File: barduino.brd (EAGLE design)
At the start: 50.3 x 47.4 mm, 28 parts, among them Q2 16MHz

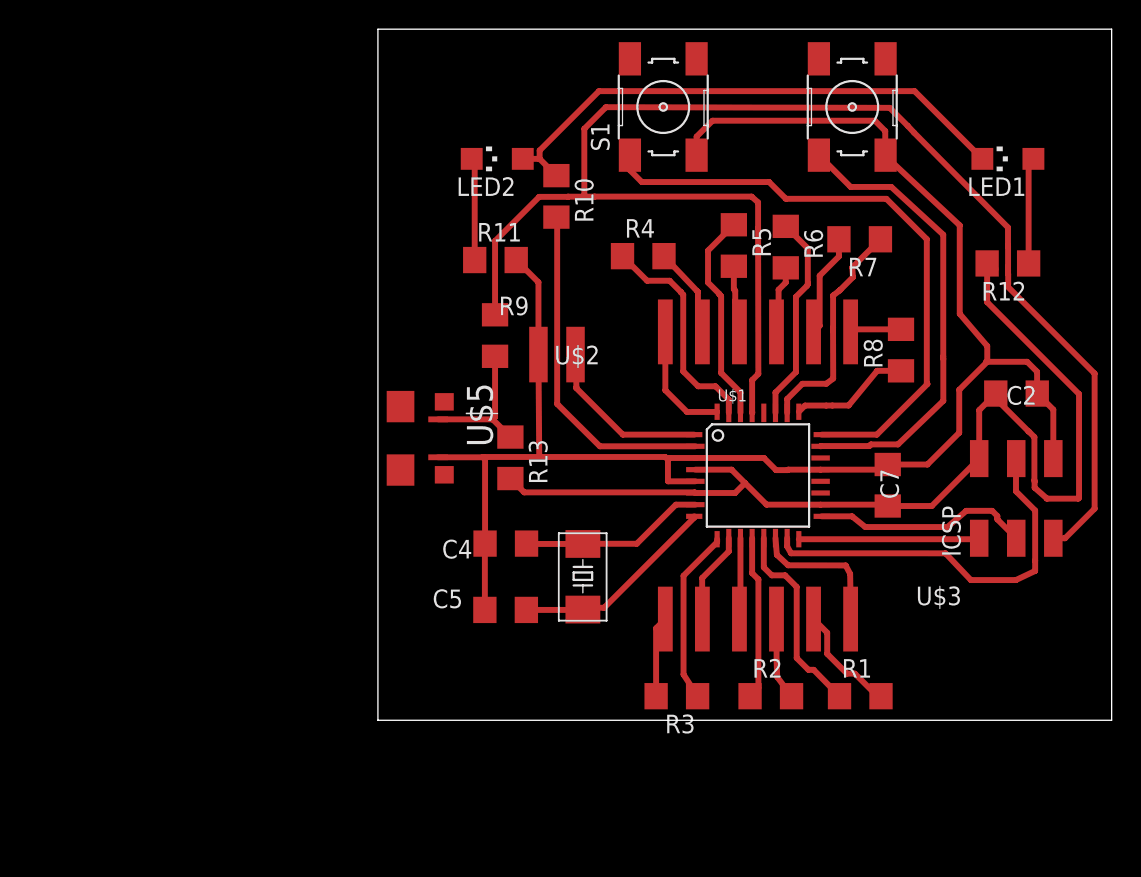
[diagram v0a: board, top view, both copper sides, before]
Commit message: replace crystal with new footprint part
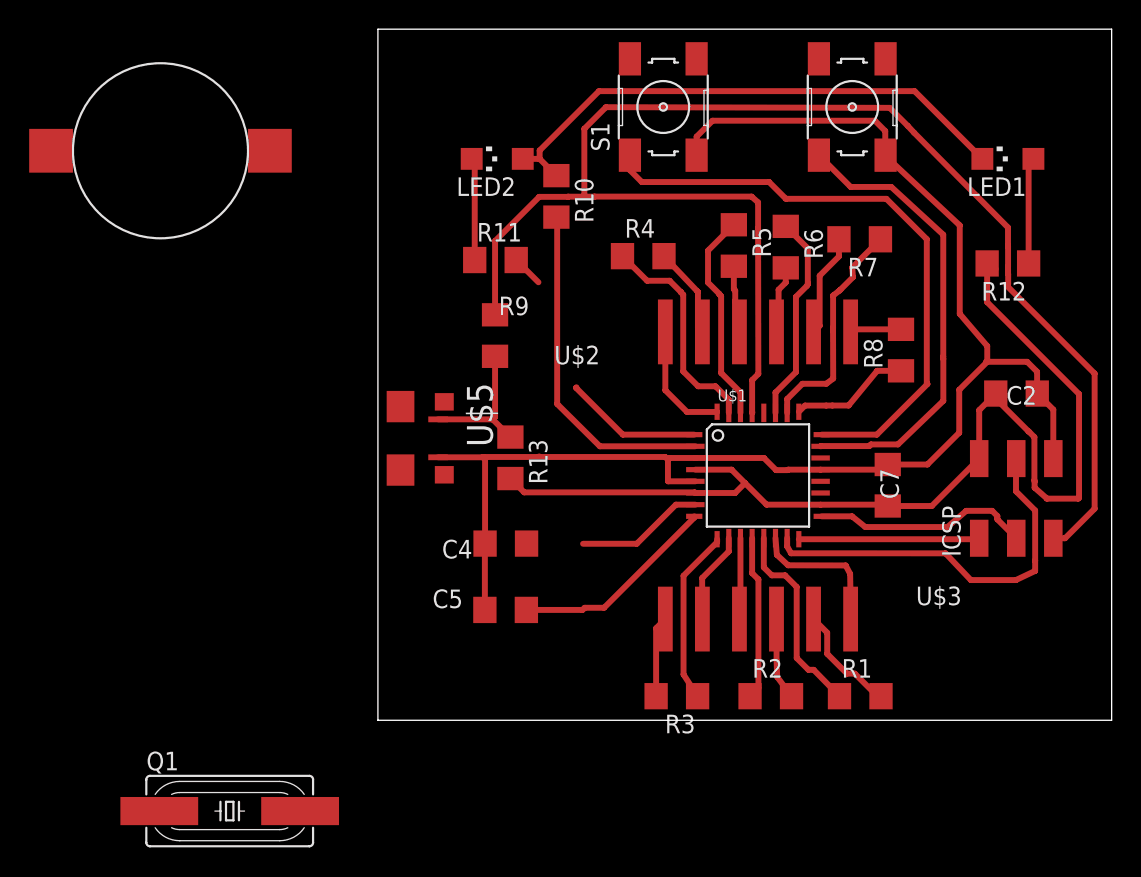
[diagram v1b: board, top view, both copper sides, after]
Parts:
- removed Q2: 16MHz, ng:CS10
- added Q1: 16MHz, crystal:HC49UP
- U$4: device 4-Digit-Clock:BUZZER -> 4-Digit-Clock:CD-1206-SMT
- moved U$4 30.6 mm to (-30.1, 51.4)
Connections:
- net PB6: now also Q1.2; no longer Q2.P$2
- net PB7: now also Q1.1; no longer Q2.P$1
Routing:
- net GND: track 115.3 -> 103.4 mm
- net PB6: track 12.7 -> 8.84 mm
- net D3: track 11.7 -> 9.47 mm
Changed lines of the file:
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@@
 </autorouter>
 <elements>
-<element name="Q2" library="ng" package="CS10" value="16MHz" x="-1.1912" y="22.19458125" smashed="yes" rot="R90">
-<attribute name="VALUE" x="2.2378" y="19.01958125" size="1.27" layer="27" ratio="10" rot="R90"/>
-</element>
 <element name="C4" library="ng" package="1206" value="18pF" x="-6.4744" y="24.42978125" smashed="yes">
 <attribute name="NAME" x="-8.7604" y="24.68378125" size="1.27" layer="25" rot="R180"/>
@@
 <element name="U$2" library="4-Digit-Clock" package="HEADER" value="HEADER" x="10.8103" y="36.7183"/>
 <element name="U$3" library="4-Digit-Clock" package="HEADER" value="HEADER" x="10.8103" y="21.4783" rot="R180"/>
-<element name="U$4" library="4-Digit-Clock" package="BUZZER" value="BUZZER" x="-2.96671875" y="37.3862625" rot="R180"/>
+<element name="U$4" library="4-Digit-Clock" package="CD-1206-SMT" value="BUZZER" x="-30.14471875" y="51.3562625" rot="R180"/>
 <element name="R1" library="resistor" library_urn="urn:adsk.eagle:library:348" package="R1206" package3d_urn="urn:adsk.eagle:package:26062/1" value="" x="17.820640625" y="13.97"/>
 <element name="R2" library="resistor" library_urn="urn:adsk.eagle:library:348" package="R1206" package3d_urn="urn:adsk.eagle:package:26062/1" value="" x="11.689078125" y="13.97"/>
@@
 <element name="U$5" library="4-Digit-Clock" package="DX4R005HJ5-PWR" value="MICRO-USB-PWR" x="-15.24" y="31.645859375" rot="R270"/>
 <element name="R13" library="resistor" library_urn="urn:adsk.eagle:library:348" package="R1206" package3d_urn="urn:adsk.eagle:package:26062/1" value="" x="-6.1595" y="30.30981875" rot="R270"/>
+<element name="Q1" library="crystal" library_urn="urn:adsk.eagle:library:204" package="HC49UP" package3d_urn="urn:adsk.eagle:package:12078/1" value="16MHz" x="-25.4" y="6.096">
+<attribute name="MF" value="" x="-25.4" y="6.096" size="1.778" layer="27" display="off"/>
+<attribute name="MPN" value="" x="-25.4" y="6.096" size="1.778" layer="27" display="off"/>
+<attribute name="OC_FARNELL" value="unknown" x="-25.4" y="6.096" size="1.778" layer="27" display="off"/>
+<attribute name="OC_NEWARK" value="unknown" x="-25.4" y="6.096" size="1.778" layer="27" display="off"/>
+</element>
 </elements>
 <signals>
@@
 <wire x1="4.761140625" y1="30.2983" x2="4.64058125" y2="30.177740625" width="0.4064" layer="1"/>
 <wire x1="19.65190625" y1="50.906009375" x2="19.558" y2="51.054" width="0.4064" layer="1"/>
-<wire x1="-4.183378125" y1="30.406540625" x2="-4.23671875" y2="37.3862625" width="0.4064" layer="1"/>
+<wire x1="-4.183378125" y1="30.406540625" x2="-37.64471875" y2="51.3562625" width="0" layer="19" extent="1-16"/>
 <wire x1="-4.183378125" y1="30.406540625" x2="-4.254496875" y2="30.3659" width="0.4064" layer="1"/>
 <wire x1="-4.254496875" y1="30.3659" x2="4.452421875" y2="30.3659" width="0.4064" layer="1"/>
@@
 <wire x1="-8.0924375" y1="30.3430375" x2="-8.016240625" y2="30.3659" width="0.4064" layer="1"/>
 <contactref element="R11" pad="2"/>
-<wire x1="-4.23671875" y1="37.3862625" x2="-4.23671875" y2="42.341403125" width="0.4064" layer="1"/>
+<wire x1="-37.64471875" y1="51.3562625" x2="-4.23671875" y2="42.341403125" width="0" layer="19" extent="1-16"/>
 <wire x1="-4.23671875" y1="42.341403125" x2="-5.76111875" y2="43.865803125" width="0.4064" layer="1"/>
 <contactref element="U$5" pad="GND"/>
@@
 </signal>
 <signal name="PB7">
-<contactref element="Q2" pad="P$1"/>
 <contactref element="C5" pad="2"/>
 <contactref element="U$1" pad="8"/>
@@
 <wire x1="6.4415" y1="26.210321875" x2="0.26161875" y2="20.030440625" width="0.4064" layer="1"/>
 <wire x1="-1.069340625" y1="20.030440625" x2="0.26161875" y2="20.030440625" width="0.4064" layer="1"/>
-<wire x1="-1.069340625" y1="20.030440625" x2="-1.1912" y2="19.90858125" width="0.4064" layer="1"/>
 <wire x1="-5.0651" y1="19.883175" x2="-1.21660625" y2="19.883175" width="0.4064" layer="1"/>
 <wire x1="-1.21660625" y1="19.883175" x2="-1.069340625" y2="20.030440625" width="0.4064" layer="1"/>
+<contactref element="Q1" pad="1"/>
+<wire x1="-5.0651" y1="19.883175" x2="-30.226" y2="6.096" width="0" layer="19" extent="1-1"/>
 </signal>
 <signal name="RESET">
@@
 </signal>
 <signal name="PB6">
-<contactref element="Q2" pad="P$2"/>
 <contactref element="C4" pad="2"/>
 <wire x1="5.18318125" y1="27.0983" x2="2.5019" y2="24.41701875" width="0.4064" layer="1"/>
 <wire x1="2.5019" y1="24.41701875" x2="-1.1785625" y2="24.41701875" width="0.4064" layer="1"/>
-<wire x1="-1.1785625" y1="24.41701875" x2="-1.1912" y2="24.40438125" width="0.4064" layer="1"/>
-<wire x1="-1.1912" y1="24.40438125" x2="-5.027" y2="24.40438125" width="0.4064" layer="1"/>
 <wire x1="-5.027" y1="24.40438125" x2="-5.0524" y2="24.42978125" width="0.4064" layer="1"/>
 <contactref element="U$1" pad="7"/>
 <wire x1="6.5177" y1="27.0983" x2="5.18318125" y2="27.0983" width="0.4064" layer="1"/>
+<contactref element="Q1" pad="2"/>
+<wire x1="-5.027" y1="24.40438125" x2="-1.1785625" y2="24.41701875" width="0" layer="19" extent="1-1"/>
+<wire x1="-20.574" y1="6.096" x2="-5.0524" y2="24.42978125" width="0" layer="19" extent="1-1"/>
 </signal>
 <signal name="D0">
@@
 <wire x1="1.548421875" y1="31.8983" x2="-1.65861875" y2="35.105340625" width="0.4064" layer="1"/>
 <wire x1="-1.65861875" y1="35.105340625" x2="-1.63321875" y2="35.143440625" width="0.4064" layer="1"/>
-<wire x1="-1.63321875" y1="35.143440625" x2="-1.69671875" y2="37.3862625" width="0.4064" layer="1"/>
+<wire x1="-1.63321875" y1="35.143440625" x2="-22.64471875" y2="51.3562625" width="0" layer="19" extent="1-16"/>
 <wire x1="6.4415" y1="31.8983" x2="1.548421875" y2="31.8983" width="0.4064" layer="1"/>
 </signal>
